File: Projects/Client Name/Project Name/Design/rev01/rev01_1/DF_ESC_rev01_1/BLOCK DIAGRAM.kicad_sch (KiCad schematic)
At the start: 0 parts

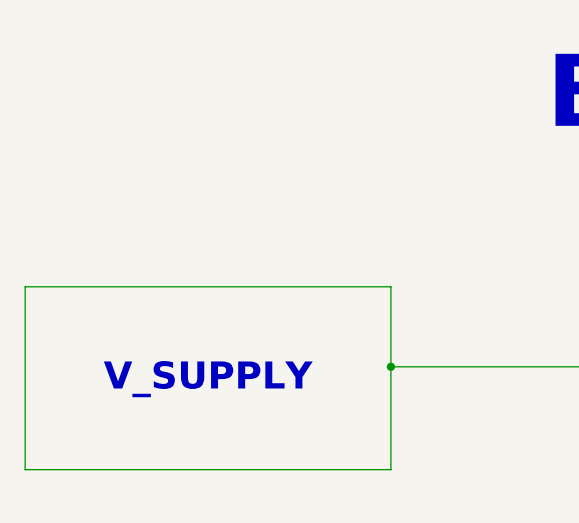
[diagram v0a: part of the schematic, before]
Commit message: Update2_1
Added Voltage range
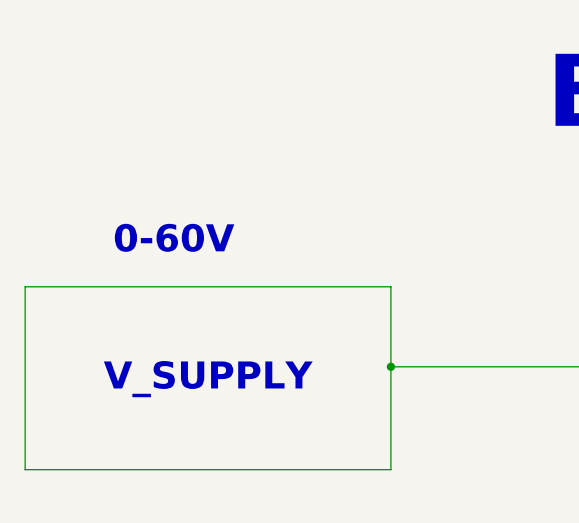
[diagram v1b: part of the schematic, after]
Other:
- note added: "0-60V"
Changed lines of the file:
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@@
+		)
+	)
+	(text "0-60V"
+		(exclude_from_sim no)
+		(at 55.88 39.37 0)
+		(effects
+			(font
+				(size 3 3)
+				(bold yes)
+			)
 		)
 	)
